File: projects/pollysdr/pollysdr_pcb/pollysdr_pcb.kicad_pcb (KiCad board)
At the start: 2 copper layers, 43.2 x 22.9 mm, 0 parts

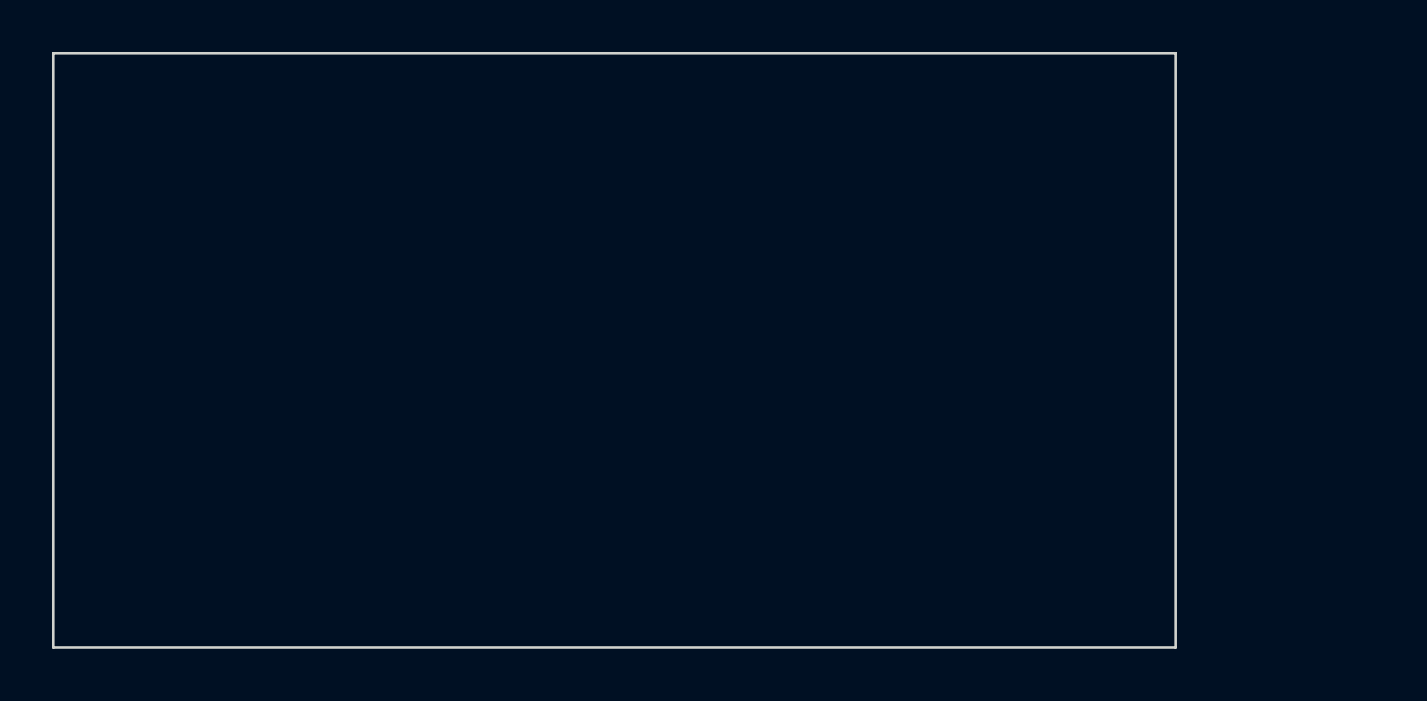
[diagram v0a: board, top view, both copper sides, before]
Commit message: Check in a basic Si2141 breakout board. Untested.
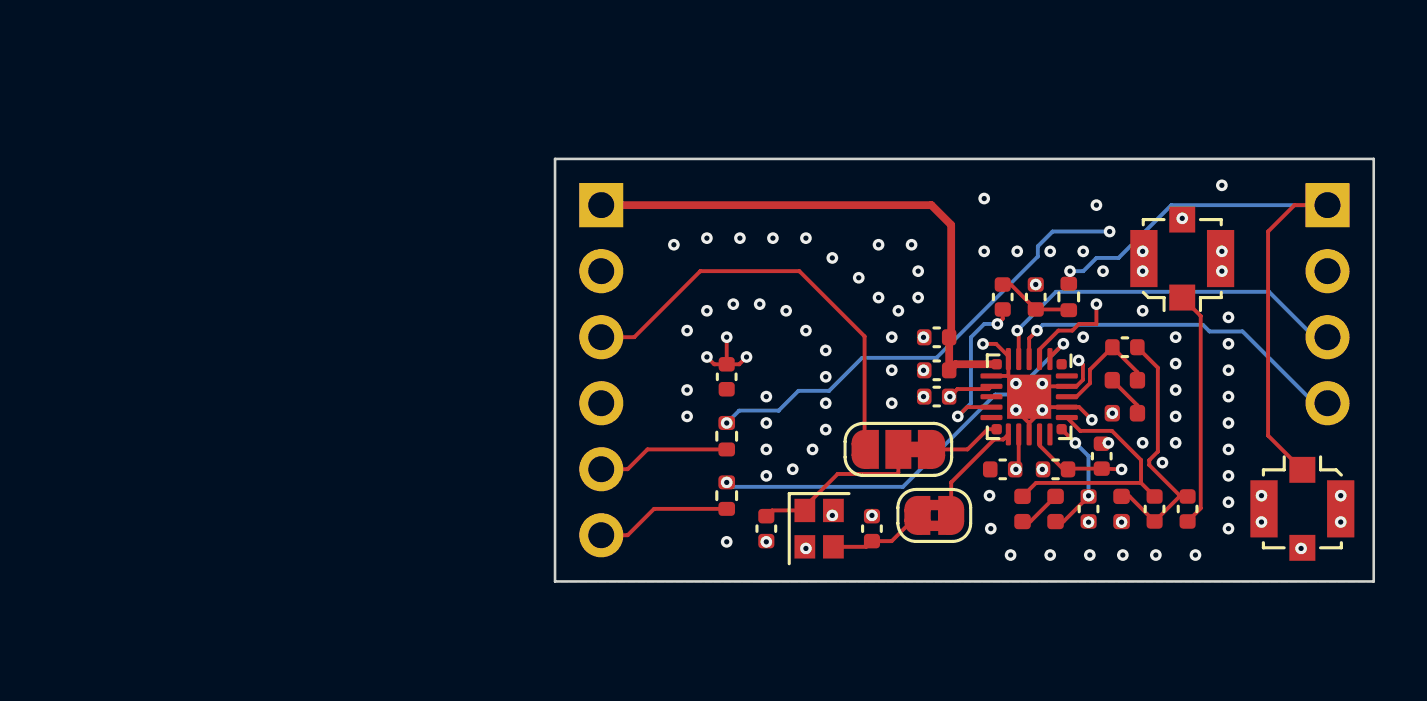
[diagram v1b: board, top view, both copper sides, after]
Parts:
- added C1: 1n, Capacitor_SMD:C_0402_1005Metric, F.Cu at (85.5, 73.4)
- added C10: 1n, Capacitor_SMD:C_0402_1005Metric, F.Cu at (89.4, 73.4)
- added C11: 30p, Capacitor_SMD:C_0402_1005Metric, F.Cu at (86.9, 67.2)
- added C12: 30p, Capacitor_SMD:C_0402_1005Metric, F.Cu at (83.5, 65.3)
- added C13: 100n, Capacitor_SMD:C_0402_1005Metric, F.Cu at (82.2, 65.3)
- added C14: 30p, Capacitor_SMD:C_0402_1005Metric, F.Cu at (73.2, 74.2)
- added C15: 30p, Capacitor_SMD:C_0402_1005Metric, F.Cu at (77.2, 74.2)
- added C2: 1u, Capacitor_SMD:C_0402_1005Metric, F.Cu at (71.6, 68.3)
- added C3: 10n, Capacitor_SMD:C_0402_1005Metric, F.Cu at (79.7, 69.1)
- added C4: 100n, Capacitor_SMD:C_0402_1005Metric, F.Cu at (84.3, 71.9)
- added C5: 10n, Capacitor_SMD:C_0402_1005Metric, F.Cu at (86.1, 71.4)
- added C6: 10n, Capacitor_SMD:C_0402_1005Metric, F.Cu at (82.2, 71.9)
- added C7: 1n, Capacitor_SMD:C_0402_1005Metric, F.Cu at (79.7, 68.1)
- added C8: 30p, Capacitor_SMD:C_0402_1005Metric, F.Cu at (88.1, 73.4)
- added C9: 1u, Capacitor_SMD:C_0402_1005Metric, F.Cu at (79.7, 66.8)
- added J1: Conn_Coaxial, Connector_Coaxial:U.FL_Molex_MCRF_73412-0110_Vertical, F.Cu at (89.2, 63.8)
- added J2: Conn_01x04, Connector_PinHeader_2.54mm:PinHeader_1x04_P2.54mm_Vertical, B.Cu at (94.7, 61.7)
- added J3: Conn_01x06, Connector_PinHeader_2.54mm:PinHeader_1x06_P2.54mm_Vertical, B.Cu at (66.8, 61.7)
- added J4: Conn_Coaxial, Connector_Coaxial:U.FL_Molex_MCRF_73412-0110_Vertical, F.Cu at (93.8, 73.4)
- added JP1: SolderJumper_3_Bridged12, Jumper:SolderJumper-3_P1.3mm_Bridged12_RoundedPad1.0x1.5mm_NumberLabels, F.Cu at (78.2, 71.1)
- added JP2: SolderJumper_2_Bridged, Jumper:SolderJumper-2_P1.3mm_Bridged2Bar_RoundedPad1.0x1.5mm, F.Cu at (79.6, 73.7)
- added L1: 270n, Inductor_SMD:L_0402_1005Metric, F.Cu at (84.3, 73.4)
- added L2: 270n, Inductor_SMD:L_0402_1005Metric, F.Cu at (83.0, 73.4)
- added L3: 270n, Inductor_SMD:L_0402_1005Metric, F.Cu at (86.8, 73.4)
- added L4: 270n, Inductor_SMD:L_0402_1005Metric, F.Cu at (86.9, 68.5)
- added L5: 270n, Inductor_SMD:L_0402_1005Metric, F.Cu at (86.9, 69.7)
- added R1: 100, Resistor_SMD:R_0402_1005Metric, F.Cu at (84.8, 65.3)
- added R2: 100, Resistor_SMD:R_0402_1005Metric, F.Cu at (71.6, 72.9)
- added R3: 100, Resistor_SMD:R_0402_1005Metric, F.Cu at (71.6, 70.6)
- added U1: ~, Custom:SiliconLabs-QFN-24-1EP_3x3mm_P0.4mm_EP1.8x1.8mm, F.Cu at (83.3, 69.1)
- added Y1: 24MHz, Crystal:Crystal_SMD_2016-4Pin_2.0x1.6mm, F.Cu at (75.2, 74.2)
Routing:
- net Net-(U1-SCL): track 0.00 -> 24.9 mm, vias 0 -> 3
- net Net-(J2-Pin_1): track 0.00 -> 23.4 mm, vias 0 -> 1
- net +1V8: track 0.00 -> 21.3 mm
- net Net-(J3-Pin_3): track 0.00 -> 16.6 mm
- net Net-(U1-SDA): track 0.00 -> 16.3 mm, vias 0 -> 2
- net /AGC1: track 0.00 -> 13.9 mm, vias 0 -> 1
- net /AGC2: track 0.00 -> 13.2 mm, vias 0 -> 1
- net Net-(C10-Pad2): track 0.00 -> 10.3 mm
- net +3V3: track 0.00 -> 9.99 mm, vias 0 -> 6
- net Net-(U1-RF_IP): track 0.00 -> 9.92 mm
- net GND: track 0.00 -> 9.55 mm, vias 0 -> 99
- net Net-(J1-In): track 0.00 -> 9.12 mm
- net Net-(JP1-C): track 0.00 -> 6.75 mm
- net Net-(U1-LIF_P): track 0.00 -> 6.57 mm, vias 0 -> 2
- net Net-(J3-Pin_6): track 0.00 -> 5.25 mm
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- added copper zone on In2.Cu, net +3V3
- added copper zone on B.Cu, net GND
- added copper zone on F.Cu, net GND
- added copper zone on In1.Cu, net GND
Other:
- board size 43.2 x 22.9 mm -> 31.5 x 16.3 mm
- copper layers 2 -> 4
